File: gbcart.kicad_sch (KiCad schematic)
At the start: 31 parts, among them J1 Conn_01x32, J2 USB_B_Micro, J3 Micro_SD_Card, U1 ATmega32U4-A, U2 74HC138, U3 74HCT1G125, U4 74LS259, U5 29F040-TSOP-SP, U6 74lxc125, U7 74HCT1G125, U8 LD3985M33R_SOT23, U9 NC7SZ08, Y1 16MHz

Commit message: Add forgotten connection to A18
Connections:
- net at U4.11 (Q6): now also U5.9 (A18)
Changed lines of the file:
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@@
+    (stroke (width 0) (type default) (color 0 0 0 0))
+  )
+  (wire (pts (xy 199.39 102.87) (xy 199.39 109.22))
     (stroke (width 0) (type default) (color 0 0 0 0))
   )
@@
     (stroke (width 0) (type default) (color 0 0 0 0))
   )
+  (wire (pts (xy 199.39 109.22) (xy 153.67 109.22))
+    (stroke (width 0) (type default) (color 0 0 0 0))
+  )

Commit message: Add LED and switch
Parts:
- added D3: LED_RGB, LED_SMD:LED_RGB_PLCC-6, symbol Device:LED_RGB
- added R10, R8, R9: 330, Resistor_SMD:R_0402_1005Metric_Pad0.72x0.64mm_HandSolder, symbol Device:R
- added R7: 10k, Resistor_SMD:R_0402_1005Metric_Pad0.72x0.64mm_HandSolder, symbol Device:R
- added SW1: SW_Push, Button_Switch_SMD:SW_SPST_FSMSM, symbol Switch:SW_Push
- R4: value 0 -> 10k
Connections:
- net +5V: now also R4.2, R7.2
- net GND: now also D3.1 (RK), D3.2 (GK), D3.3 (BK), SW1.1; no longer R4.2
- net at R6.2, U1.13 (~{RESET}): now also R7.1
- net at R4.1, U1.33 (~{HWB}/PE2): now also SW1.2
- net at U1.28 (PB4): now also R8.2
- net at U1.29 (PB5): now also R9.2
- net at U1.30 (PB6): now also R10.2
- new net: D3.5 (GA), R9.1
- new net: D3.4 (BA), R8.1
- new net: D3.6 (RA), R10.1
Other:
- moved on the sheet: R4

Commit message: Mark proper 74 family
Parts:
- U4: value 74LS259 -> 74HC259
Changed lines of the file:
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@@
       (effects (font (size 1.27 1.27)) (justify left))
     )
-    (property "Value" "74LS259" (id 1) (at 142.9894 88.9 0)
+    (property "Value" "74HC259" (id 1) (at 142.9894 88.9 0)
       (effects (font (size 1.27 1.27)) (justify left))
     )
@@
     )
     (path "/10673c6d-0fa1-4b16-8dab-ed0f08225d3e"
-      (reference "U4") (unit 1) (value "74LS259") (footprint "Package_SO:SO-16_3.9x9.9mm_P1.27mm")
+      (reference "U4") (unit 1) (value "74HC259") (footprint "Package_SO:SO-16_3.9x9.9mm_P1.27mm")
     )
     (path "/840b8156-7ec7-4a82-81b5-523223ee7684"

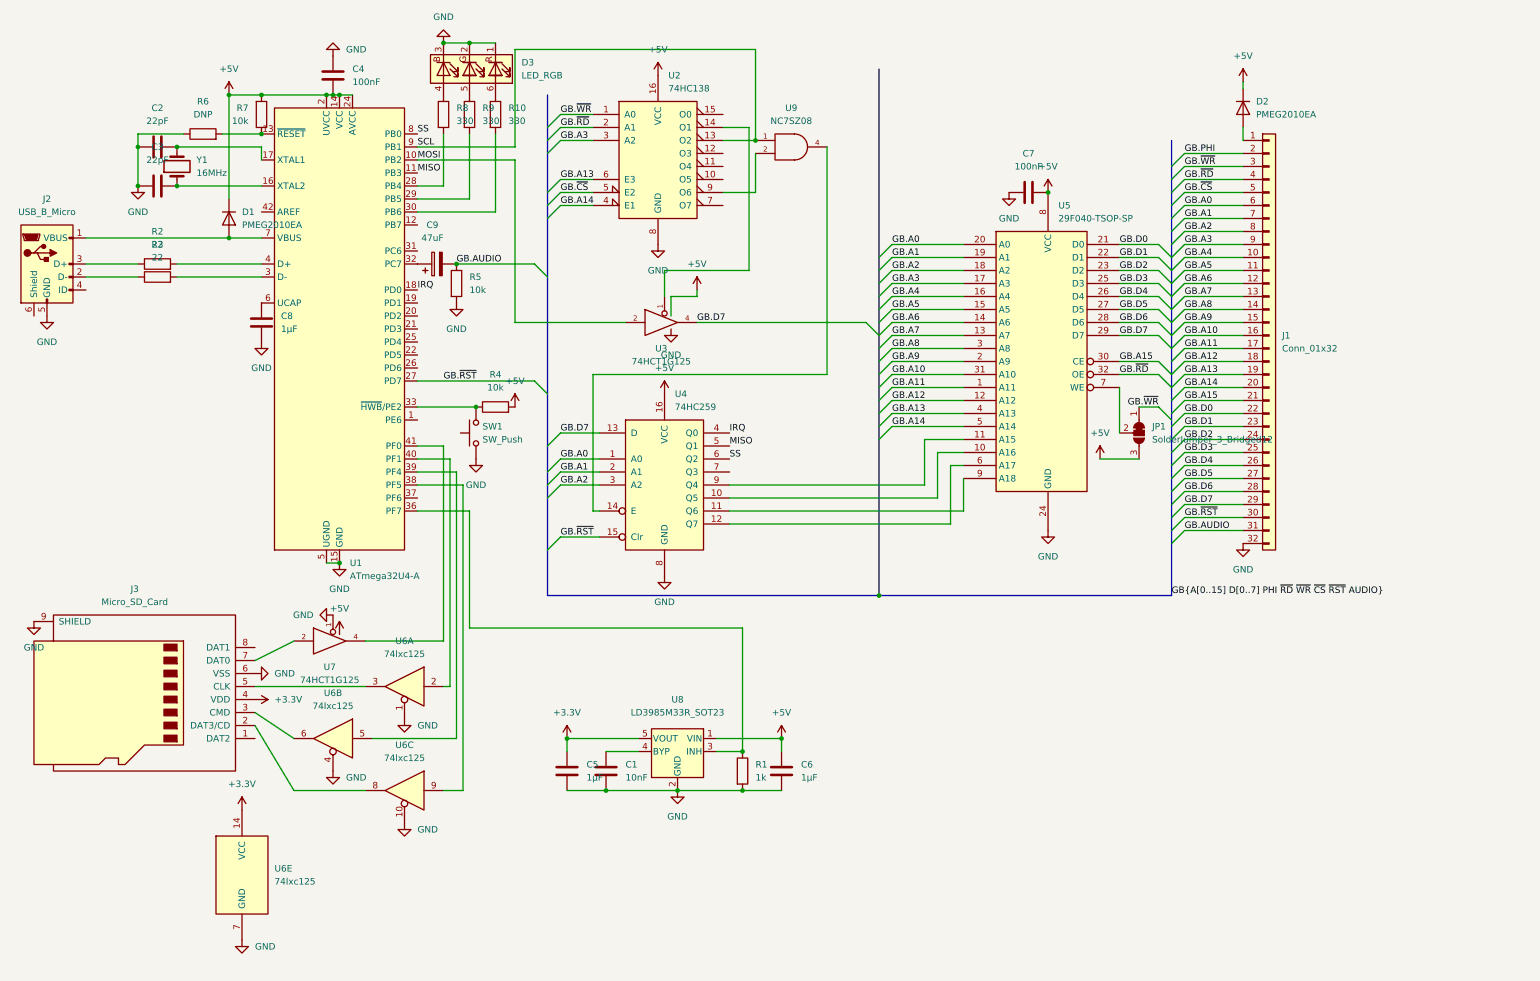
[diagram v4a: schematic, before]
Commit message: choose diferent mcu
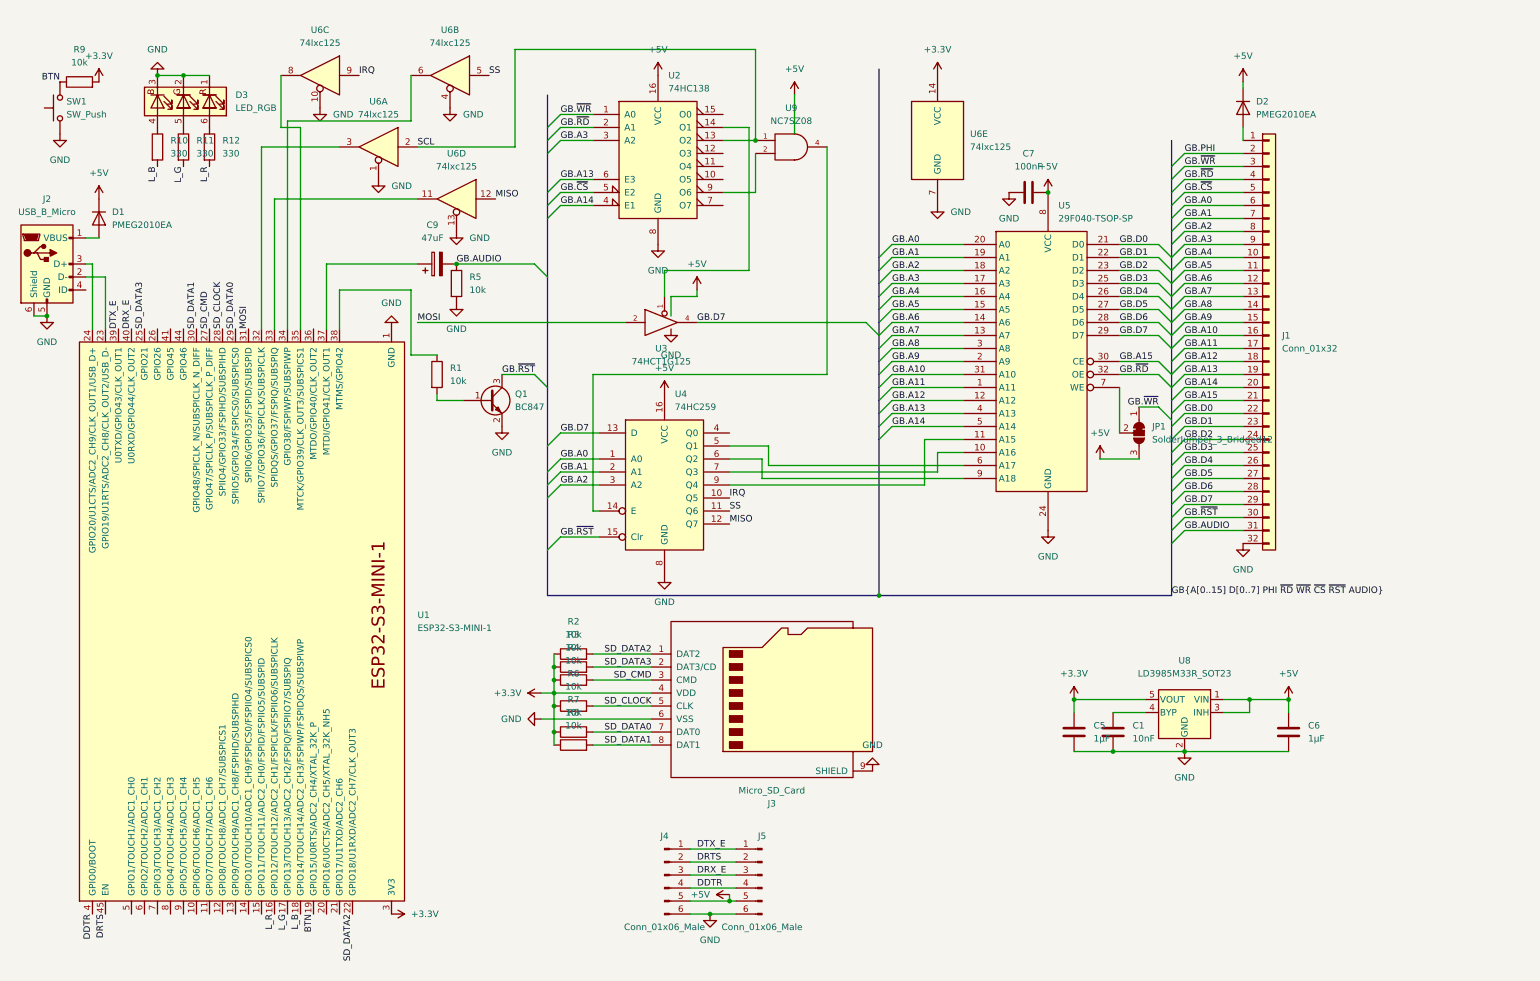
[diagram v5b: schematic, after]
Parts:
- removed C2, C3: 22pF, Capacitor_SMD:C_0805_2012Metric_Pad1.18x1.45mm_HandSolder, symbol Device:C
- removed C4: 100nF, Capacitor_SMD:C_0805_2012Metric_Pad1.18x1.45mm_HandSolder, symbol Device:C
- removed C8: 1µF, Capacitor_SMD:C_0805_2012Metric_Pad1.18x1.45mm_HandSolder, symbol Device:C
- removed U1: ATmega32U4-A, Package_QFP:TQFP-44_10x10mm_P0.8mm, symbol MCU_Microchip_ATmega:ATmega32U4-A
- removed U7: 74HCT1G125, Package_TO_SOT_SMD:SOT-353_SC-70-5_Handsoldering, symbol 74xGxx:74AHC1G125
- removed Y1: 16MHz, Crystal:Crystal_SMD_HC49-SD_HandSoldering, symbol Device:Crystal
- added J4: Conn_01x06_Male, Connector_PinHeader_2.54mm:PinHeader_2x03_P2.54mm_Vertical_SMD, symbol Connector:Conn_01x06_Male
- added J5: Conn_01x06_Male, Connector_PinHeader_2.54mm:PinHeader_2x03_P2.54mm_Horizontal, symbol Connector:Conn_01x06_Male
- added Q1: BC847, Package_TO_SOT_SMD:SOT-23, symbol Transistor_BJT:BC847
- added R11, R12: 330, Resistor_SMD:R_0402_1005Metric_Pad0.72x0.64mm_HandSolder, symbol Device:R
- added U1: ESP32-S3-MINI-1, Espressif:ESP32-S3-MINI-1, symbol Espressif:ESP32-S3-MINI-1
- added unit 3 of U6
- R1: value 1k -> 10k
- R2, R3: value 22 -> 10k
- R6: value DNP -> 10k
- R8, R9: value 330 -> 10k
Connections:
- net +3.3V: now also R2.1, R3.1, R4.1, R6.1, R7.1, R8.1, R9.2, U1.3 (3V3)
- net +5V: now also U8.3 (INH), J4.5 (Pin_5), J5.5 (Pin_5); no longer R4.2, R7.2
- net GB.~{RST}: now also Q1.3 (C)
- net GND: now also J2.6 (Shield), U6.1, U6.13, U6.4, J4.6 (Pin_6), J5.6 (Pin_6), Q1.2 (E), U1.1 (GND), U1.2 (GND), U1.42 (GND), U1.43 (GND), U1.46 (GND), U1.47 (GND), U1.48 (GND), U1.49 (GND), U1.50 (GND), U1.51 (GND), U1.52 (GND), U1.53 (GND), U1.54 (GND), U1.55 (GND), U1.56 (GND), U1.57 (GND), U1.58 (GND), U1.59 (GND), U1.60 (GND), U1.61 (GND), U1.62 (GND), U1.63 (GND), U1.64 (GND), U1.65 (GND), U6.10; no longer R1.2, R6.1, U6.1, U6.10, U6.4
- net IRQ: now also U4.10 (Q5), U6.9; no longer U4.4 (Q0)
- net MISO: now also U4.12 (Q7), U6.12; no longer U4.5 (Q1)
- net MOSI: now also U1.31 (SPIIO6/GPIO35/FSPID/SUBSPID)
- net SCL: now also U6.2
- net SS: now also U4.11 (Q6), U6.5; no longer U4.6 (Q2)
- net at J2.3 (D+): now also U1.24 (GPIO20/U1CTS/ADC2_CH9/CLK_OUT1/USB_D+); no longer R2.1
- net SD_DATA2: now reaches R2.2
- net SD_DATA2: now also J3.1 (DAT2), U1.22 (GPIO18/U1RXD/ADC2_CH7/CLK_OUT3)
- net SD_DATA0: now reaches J3.7 (DAT0)
- net SD_DATA0: now also R7.2, U1.29 (SPIIO5/GPIO34/FSPICS0/SUBSPICS0)
- net at U5.10 (A16): now also U4.7 (Q3); no longer U4.10 (Q5)
- net at U5.9 (A18): now also U4.6 (Q2); no longer U4.11 (Q6)
- net at U5.6 (A17): now also U4.5 (Q1); no longer U4.12 (Q7)
- net at D3.5 (GA): now also R11.1; no longer R9.1
- net at R1.1: now also U1.38 (MTMS/GPIO42); no longer U8.3 (INH)
- net at D3.4 (BA): now also R10.1; no longer R8.1
- net at D3.6 (RA): now also R12.1; no longer R10.1
- net at J2.2 (D-): now also U1.23 (GPIO19/U1RTS/ADC2_CH8/CLK_OUT2/USB_D-); no longer R3.1
- net SD_DATA3: now reaches R3.2
- net SD_DATA3: now also J3.2 (DAT3/CD), U1.25 (GPIO21)
- net at C9.1: now also U1.37 (MTDI/GPIO41/CLK_OUT1)
- net SD_CLOCK: now reaches J3.5 (CLK)
- net SD_CLOCK: now also R6.2, U1.28 (SPIIO4/GPIO33/FSPIHD/SUBSPIHD); no longer U6.3
- net SD_DATA1: now reaches R8.2
- net SD_DATA1: now also J3.8 (DAT1), U1.30 (GPIO48/SPICLK_N/SUBSPICLK_N_DIFF)
- net BTN: now reaches SW1.2
- net BTN: now also R9.1, U1.19 (GPIO15/U0RTS/ADC2_CH4/XTAL_32K_P); no longer R4.1
- net L_B: now reaches R10.2
- net L_B: now also U1.18 (GPIO14/TOUCH14/ADC2_CH3/FSPIWP/FSPIDQS/SUBSPIWP)
- net SD_CMD: now reaches J3.3 (CMD)
- net SD_CMD: now also R4.2, U1.27 (GPIO47/SPICLK_P/SUBSPICLK_P_DIFF); no longer U6.6
- new net: Q1.1 (B), R1.2
- new net: U1.34 (GPIO38/FSPIWP/SUBSPIWP), U6.6
- new net: U1.35 (MTCK/GPIO39/CLK_OUT3/SUBSPICS1), U6.8
- new net: U1.33 (SPIDQS/GPIO37/FSPIQ/SUBSPIQ), U6.11
- new net: U1.32 (SPIIO7/GPIO36/FSPICLK/SUBSPICLK), U6.3
- new net DDTR: J4.4 (Pin_4), J5.4 (Pin_4), U1.4 (GPIO0/BOOT)
- new net DRTS: J4.2 (Pin_2), J5.2 (Pin_2), U1.45 (EN)
- new net DRX_E: J4.3 (Pin_3), J5.3 (Pin_3), U1.40 (U0RXD/GPIO44/CLK_OUT2)
- new net DTX_E: J4.1 (Pin_1), J5.1 (Pin_1), U1.39 (U0TXD/GPIO43/CLK_OUT1)
- new net L_G: R11.2, U1.17 (GPIO13/TOUCH13/ADC2_CH2/FSPIQ/FSPIIO7/SUBSPIQ)
- new net L_R: R12.2, U1.16 (GPIO12/TOUCH12/ADC2_CH1/FSPICLK/FSPIIO6/SUBSPICLK)
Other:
- moved on the sheet: C1, C5, C6, D1, J3, U6A, U6B, U6D, U6E, U8

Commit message: Move connections to avalible on esp32-s3-DevkitC
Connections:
- net SD_CLOCK: now also U1.13 (GPIO9/TOUCH9/ADC1_CH8/FSPIHD/SUBSPIHD); no longer U1.28 (SPIIO4/GPIO33/FSPIHD/SUBSPIHD)
- net SD_DATA0: now also U1.12 (GPIO8/TOUCH8/ADC1_CH7/SUBSPICS1); no longer U1.29 (SPIIO5/GPIO34/FSPICS0/SUBSPICS0)
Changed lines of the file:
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@@
+    (effects (font (size 1.27 1.27)) (justify right bottom))
+  )
+  (label "SD_DATA0" (at 54.61 187.96 270)
     (effects (font (size 1.27 1.27)) (justify right bottom))
   )
@@
     (effects (font (size 1.27 1.27)) (justify right bottom))
   )
-  (label "SD_DATA0" (at 57.15 73.66 90)
-    (effects (font (size 1.27 1.27)) (justify left bottom))
-  )
   (label "SD_DATA2" (at 80.01 187.96 270)
     (effects (font (size 1.27 1.27)) (justify right bottom))
@@
     (effects (font (size 1.27 1.27)) (justify left bottom))
   )
-  (label "SD_CLOCK" (at 54.61 73.66 90)
-    (effects (font (size 1.27 1.27)) (justify left bottom))
-  )
   (label "GB.A11" (at 185.42 85.09 0)
     (effects (font (size 1.27 1.27)) (justify left bottom))
   )
+  (label "SD_CLOCK" (at 57.15 187.96 270)
+    (effects (font (size 1.27 1.27)) (justify right bottom))
+  )
   (label "SD_CLOCK" (at 138.43 147.32 180)

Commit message: Move reset to seperate IO pin
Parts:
- added U7: 74HCT1G125, Package_TO_SOT_SMD:SOT-353_SC-70-5_Handsoldering, symbol 74xGxx:74AHC1G125
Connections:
- net +5V: now also U7.5 (VCC)
- net GB.~{RST}: no longer U4.15 (Clr)
- net GND: now also U7.1, U7.3 (GND)
- net at U1.36 (MTDO/GPIO40/CLK_OUT2): now also U7.2
- new net: U4.15 (Clr), U7.4
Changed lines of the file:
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@@
-    (stroke (width 0) (type default) (color 0 0 0 0))
-  )
-  (bus_entry (at 118.11 116.84) (size 2.54 -2.54)
     (stroke (width 0) (type default) (color 0 0 0 0))
   )
@@
     (stroke (width 0) (type default) (color 0 0 0 0))
   )
-  (wire (pts (xy 120.65 114.3) (xy 128.27 114.3))
-    (stroke (width 0) (type default) (color 0 0 0 0))
-  )
   (wire (pts (xy 92.71 48.26) (xy 64.77 48.26))
     (stroke (width 0) (type default) (color 0 0 0 0))
@@
     (stroke (width 0) (type default) (color 0 0 0 0))
   )
+  (wire (pts (xy 92.71 114.3) (xy 92.71 64.77))
+    (stroke (width 0) (type default) (color 0 0 0 0))
+  )
   (wire (pts (xy 119.38 137.16) (xy 119.38 139.7))
     (stroke (width 0) (type default) (color 0 0 0 0))
@@
     (stroke (width 0) (type default) (color 0 0 0 0))
   )
+  (wire (pts (xy 114.3 109.22) (xy 109.22 109.22))
+    (stroke (width 0) (type default) (color 0 0 0 0))
+  )
   (wire (pts (xy 185.42 85.09) (xy 199.39 85.09))
     (stroke (width 0) (type default) (color 0 0 0 0))
@@
     (stroke (width 0) (type default) (color 0 0 0 0))
   )
+  (wire (pts (xy 72.39 64.77) (xy 72.39 73.66))
+    (stroke (width 0) (type default) (color 0 0 0 0))
+  )
   (wire (pts (xy 229.87 57.15) (xy 237.49 57.15))
     (stroke (width 0) (type default) (color 0 0 0 0))
@@
     (stroke (width 0) (type default) (color 0 0 0 0))
   )
-  (bus (pts (xy 118.11 106.68) (xy 118.11 116.84))
-    (stroke (width 0) (type default) (color 0 0 0 0))
-  )
   (wire (pts (xy 242.57 110.49) (xy 254 110.49))
     (stroke (width 0) (type default) (color 0 0 0 0))
@@
     (stroke (width 0) (type default) (color 0 0 0 0))
   )
+  (wire (pts (xy 100.33 114.3) (xy 92.71 114.3))
+    (stroke (width 0) (type default) (color 0 0 0 0))
+  )
   (wire (pts (xy 120.65 46.99) (xy 127 46.99))
     (stroke (width 0) (type default) (color 0 0 0 0))
@@
     (stroke (width 0) (type default) (color 0 0 0 0))
   )
+  (wire (pts (xy 114.3 114.3) (xy 128.27 114.3))
+    (stroke (width 0) (type default) (color 0 0 0 0))
+  )
   (wire (pts (xy 119.38 144.78) (xy 138.43 144.78))
     (stroke (width 0) (type default) (color 0 0 0 0))
@@
     (stroke (width 0) (type default) (color 0 0 0 0))
   )
+  (wire (pts (xy 109.22 109.22) (xy 109.22 113.03))
+    (stroke (width 0) (type default) (color 0 0 0 0))
+  )
   (bus (pts (xy 182.88 92.71) (xy 182.88 95.25))
     (stroke (width 0) (type default) (color 0 0 0 0))
@@
     (stroke (width 0) (type default) (color 0 0 0 0))
   )
+  (wire (pts (xy 92.71 64.77) (xy 72.39 64.77))
+    (stroke (width 0) (type default) (color 0 0 0 0))
+  )
   (bus (pts (xy 182.88 69.85) (xy 182.88 72.39))
     (stroke (width 0) (type default) (color 0 0 0 0))
@@
     (stroke (width 0) (type default) (color 0 0 0 0))
   )
-  (wire (pts (xy 92.71 72.39) (xy 133.35 72.39))
+  (wire (pts (xy 106.68 72.39) (xy 133.35 72.39))
     (stroke (width 0) (type default) (color 0 0 0 0))
   )
@@
     (stroke (width 0) (type default) (color 0 0 0 0))
   )
-  (bus (pts (xy 118.11 116.84) (xy 118.11 125.73))
+  (bus (pts (xy 118.11 106.68) (xy 118.11 125.73))
     (stroke (width 0) (type default) (color 0 0 0 0))
   )
@@
     (effects (font (size 1.27 1.27)) (justify left bottom))
   )
-  (label "GB.~{RST}" (at 120.65 114.3 0)
-    (effects (font (size 1.27 1.27)) (justify left bottom))
-  )
   (label "GB.A3" (at 185.42 64.77 0)
     (effects (font (size 1.27 1.27)) (justify left bottom))
@@
     (effects (font (size 1.27 1.27)) (justify left bottom))
   )
-  (label "MOSI" (at 92.71 72.39 0)
+  (label "MOSI" (at 106.68 72.39 0)
     (effects (font (size 1.27 1.27)) (justify left bottom))
   )
@@
     )
     (property "Datasheet" "" (id 3) (at 262.89 146.05 0)
+      (effects (font (size 1.27 1.27)) hide)
+    )
+    (pin "1")
+  )
+  (symbol (lib_id "power:+5V") (at 114.3 109.22 0) (unit 1)
+    (in_bom yes) (on_board yes) (fields_autoplaced)
+    (property "Reference" "#PWR0114" (id 0) (at 114.3 113.03 0)
+      (effects (font (size 1.27 1.27)) hide)
+    )
+    (property "Value" "+5V" (id 1) (at 114.3 104.14 0))
+    (property "Footprint" "" (id 2) (at 114.3 109.22 0)
+      (effects (font (size 1.27 1.27)) hide)
+    )
+    (property "Datasheet" "" (id 3) (at 114.3 109.22 0)
       (effects (font (size 1.27 1.27)) hide)
     )
@@
     (pin "1")
   )
+  (symbol (lib_id "power:GND") (at 107.95 109.22 180) (unit 1)
+    (in_bom yes) (on_board yes) (fields_autoplaced)
+    (property "Reference" "#PWR?" (id 0) (at 107.95 102.87 0)
+      (effects (font (size 1.27 1.27)) hide)
+    )
+    (property "Value" "GND" (id 1) (at 107.95 104.14 0))
+    (property "Footprint" "" (id 2) (at 107.95 109.22 0)
+      (effects (font (size 1.27 1.27)) hide)
+    )
+    (property "Datasheet" "" (id 3) (at 107.95 109.22 0)
+      (effects (font (size 1.27 1.27)) hide)
+    )
+    (pin "1")
+  )
   (symbol (lib_id "Connector:Conn_01x06_Male") (at 160.02 180.34 0) (mirror y) (unit 1)
     (in_bom yes) (on_board yes) (fields_autoplaced)
@@
     )
     (pin "1")
+  )
+  (symbol (lib_id "74xGxx:74AHC1G125") (at 107.95 114.3 0) (unit 1)
+    (in_bom yes) (on_board yes) (fields_autoplaced)
+    (property "Reference" "U7" (id 0) (at 107.315 119.38 0))
+    (property "Value" "74HCT1G125" (id 1) (at 107.315 121.92 0))
+    (property "Footprint" "Package_TO_SOT_SMD:SOT-353_SC-70-5_Handsoldering" (id 2) (at 107.95 114.3 0)
+      (effects (font (size 1.27 1.27)) hide)
+    )
+    (property "Datasheet" "" (id 3) (at 107.95 114.3 0)
+      (effects (font (size 1.27 1.27)) hide)
+    )
+    (pin "1")
+    (pin "2")
+    (pin "3")
+    (pin "4")
+    (pin "5")
   )
   (symbol (lib_id "power:+3.3V") (at 220.98 146.05 0) (unit 1)
@@
     (pin "1")
   )
+  (symbol (lib_id "power:GND") (at 109.22 115.57 0) (unit 1)
+    (in_bom yes) (on_board yes) (fields_autoplaced)
+    (property "Reference" "#PWR0115" (id 0) (at 109.22 121.92 0)
+      (effects (font (size 1.27 1.27)) hide)
+    )
+    (property "Value" "GND" (id 1) (at 109.22 120.65 0))
+    (property "Footprint" "" (id 2) (at 109.22 115.57 0)
+      (effects (font (size 1.27 1.27)) hide)
+    )
+    (property "Datasheet" "" (id 3) (at 109.22 115.57 0)
+      (effects (font (size 1.27 1.27)) hide)
+    )
+    (pin "1")
+  )
   (symbol (lib_id "power:+5V") (at 215.9 46.99 0) (unit 1)
     (in_bom yes) (on_board yes) (fields_autoplaced)
@@
       (reference "#PWR0113") (unit 1) (value "GND") (footprint "")
     )
+    (path "/1d0f89b8-f4ec-4cee-9232-9b319a7d8520"
+      (reference "#PWR0114") (unit 1) (value "+5V") (footprint "")
+    )
+    (path "/e5801591-ba6b-4c64-bc67-080c5d81fd2b"
+      (reference "#PWR0115") (unit 1) (value "GND") (footprint "")
+    )
     (path "/ca041cb5-ed6e-445e-8b81-74d624421f60"
       (reference "#PWR0116") (unit 1) (value "GND") (footprint "")
@@
       (reference "#PWR0119") (unit 1) (value "GND") (footprint "")
     )
+    (path "/9cee09a3-48cb-4ab6-bee5-1332d5233181"
+      (reference "#PWR?") (unit 1) (value "GND") (footprint "")
+    )
     (path "/2d349485-4630-4d56-9137-2d98b8ea5904"
       (reference "C1") (unit 1) (value "10nF") (footprint "Capacitor_SMD:C_0805_2012Metric_Pad1.18x1.45mm_HandSolder")
@@
       (reference "U6") (unit 5) (value "74lxc125") (footprint "Package_SO:SO-14_3.9x8.65mm_P1.27mm")
     )
+    (path "/c15b7d51-a146-40d1-bfca-65ff2e342f8e"
+      (reference "U7") (unit 1) (value "74HCT1G125") (footprint "Package_TO_SOT_SMD:SOT-353_SC-70-5_Handsoldering")
+    )
     (path "/4ca30664-8f89-4f4c-be41-6735a62d43c6"
